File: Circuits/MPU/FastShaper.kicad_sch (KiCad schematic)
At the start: 34 parts, among them U35 ADA4805-2ARMZ, U36 ADA4805-2ARMZ

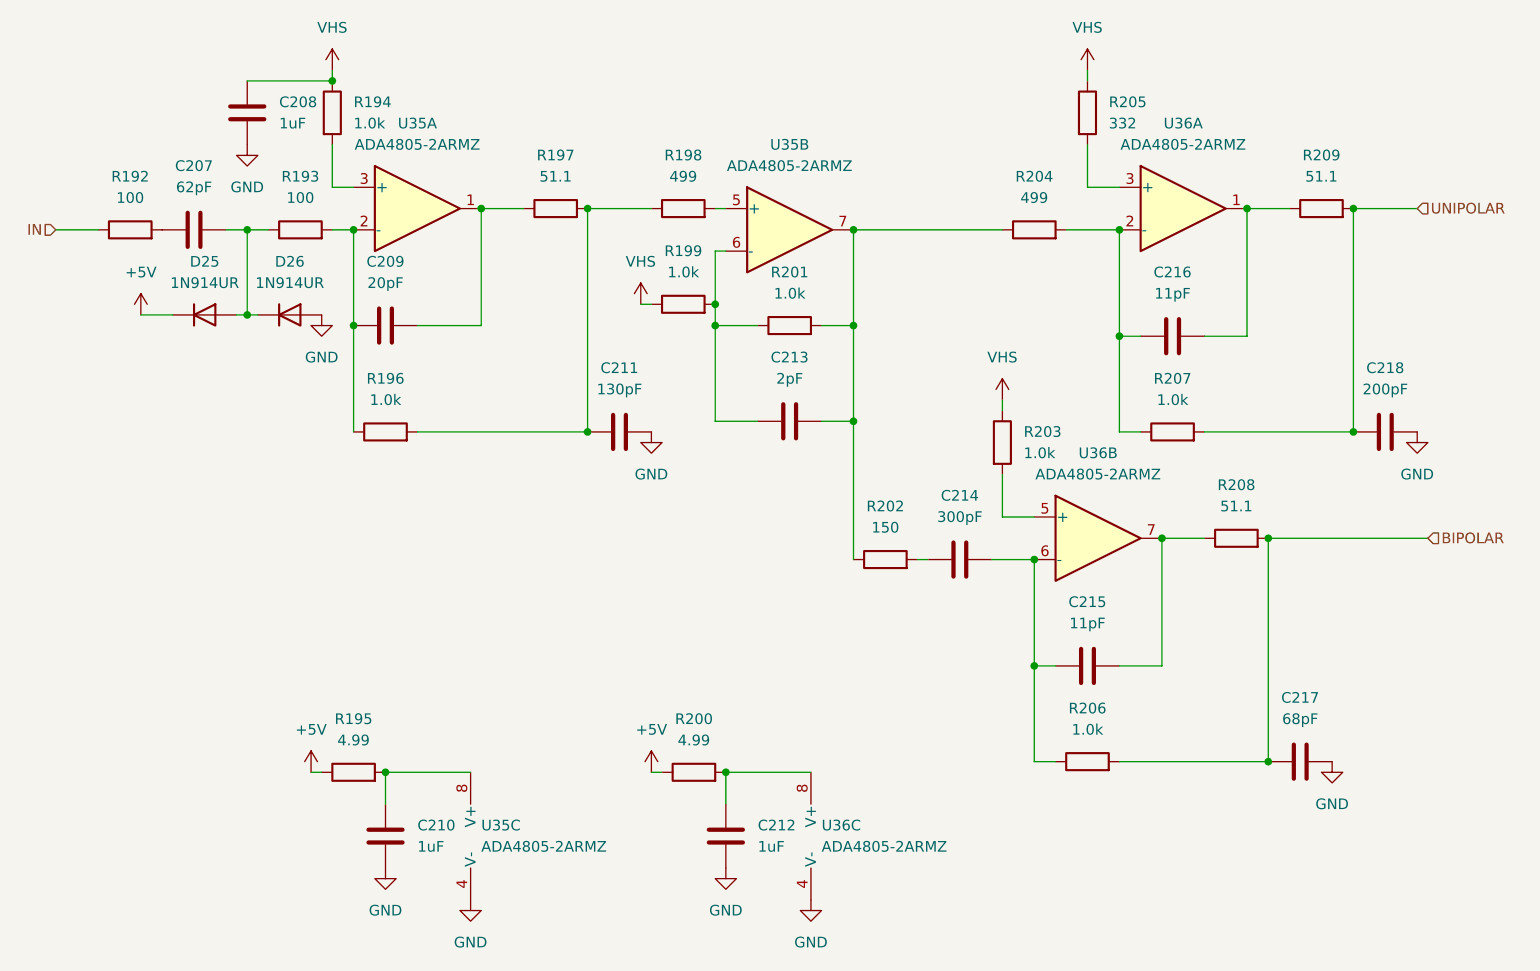
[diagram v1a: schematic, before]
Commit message: Files changed due to KiCAD update
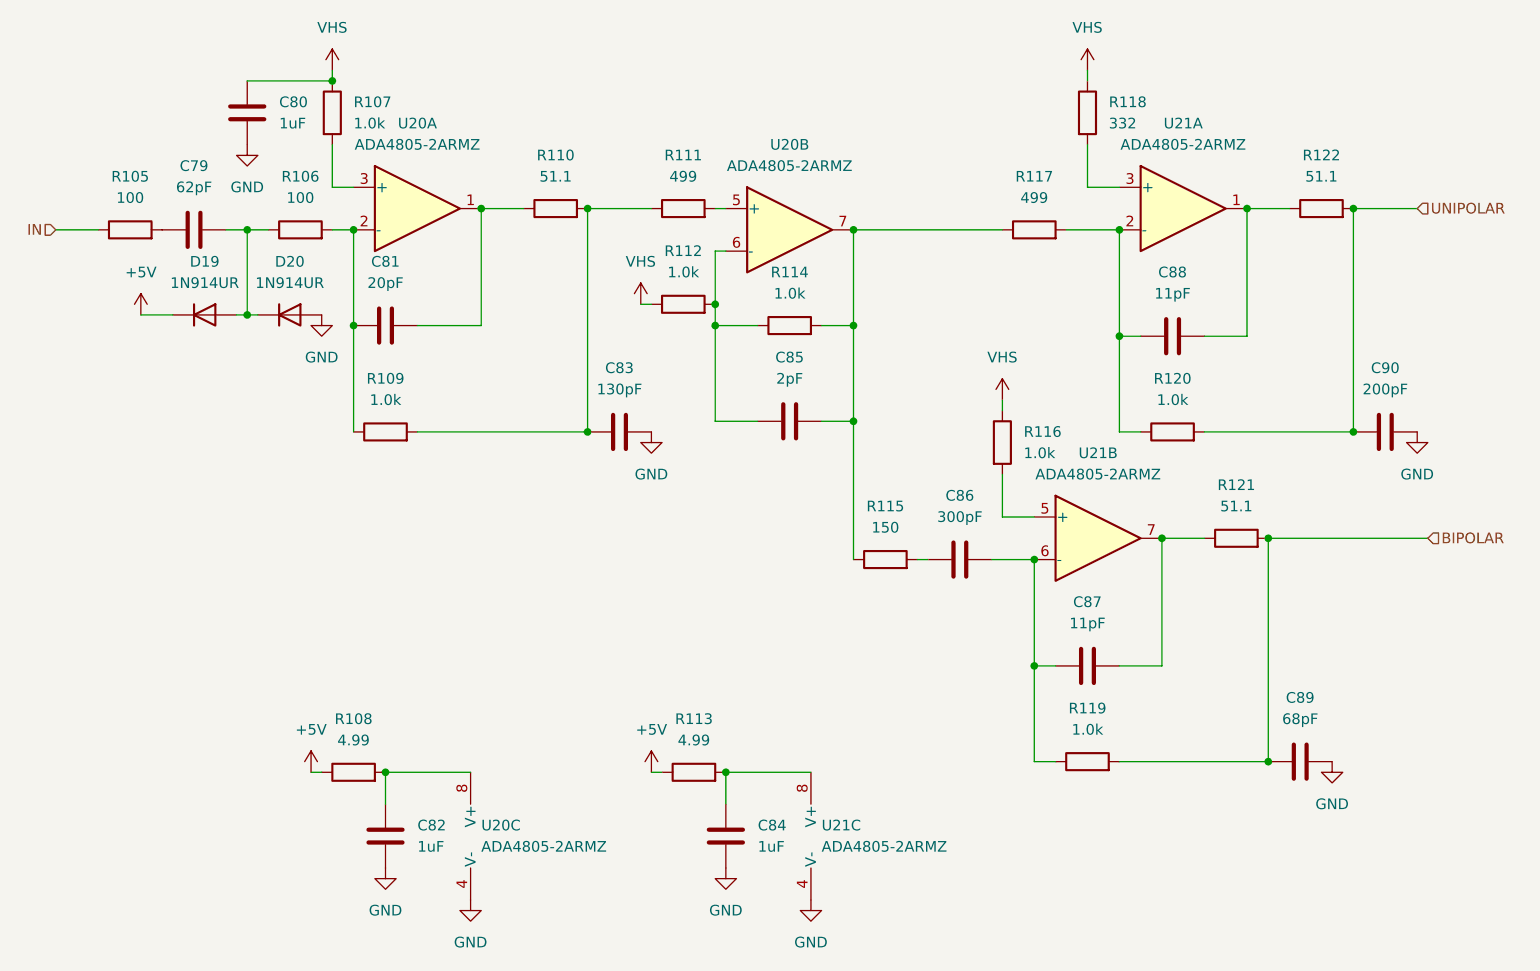
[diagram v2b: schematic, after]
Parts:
- renumbered C207 to C79, C208 to C80, C209 to C81, C210 to C82, C211 to C83, C212 to C84, C213 to C85, C214 to C86, C215 to C87, C216 to C88, C217 to C89, C218 to C90, D25 to D19, D26 to D20, R192 to R105, R193 to R106, R194 to R107, R195 to R108, R196 to R109, R197 to R110, R198 to R111, R199 to R112, R200 to R113, R201 to R114, R202 to R115, R203 to R116, R204 to R117, R205 to R118, R206 to R119, R207 to R120, R208 to R121, R209 to R122, U35 to U20, U36 to U21
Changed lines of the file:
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@@
 (kicad_sch
-	(version 20231120)
+	(version 20250114)
 	(generator "eeschema")
-	(generator_version "8.0")
+	(generator_version "9.0")
 	(paper "USLetter")
 	(title_block
@@
 		(shape input)
 		(at 204.47 66.04 0)
-		(fields_autoplaced yes)
 		(effects
 			(font
@@
 		(shape input)
 		(at 41.91 68.58 180)
-		(fields_autoplaced yes)
 		(effects
 			(font
@@
 		(shape input)
 		(at 205.74 105.41 0)
-		(fields_autoplaced yes)
 		(effects
 			(font
@@
 		(dnp no)
 		(fields_autoplaced yes)
-		(property "Reference" "D26"
+		(property "Reference" "D20"
 			(at 69.85 72.39 0)
 			(effects
@@
 		(dnp no)
 		(fields_autoplaced yes)
-		(property "Reference" "U35"
+		(property "Reference" "U20"
 			(at 85.09 55.88 0)
 			(effects
@@
 		(dnp no)
 		(fields_autoplaced yes)
-		(property "Reference" "#PWR0309"
+		(property "Reference" "#PWR0191"
 			(at 132.08 154.94 0)
 			(effects
@@
 		(dnp no)
 		(fields_autoplaced yes)
-		(property "Reference" "#PWR0298"
+		(property "Reference" "#PWR0180"
 			(at 52.07 82.55 0)
 			(effects
@@
 		(dnp no)
 		(fields_autoplaced yes)
-		(property "Reference" "#PWR0310"
+		(property "Reference" "#PWR0192"
 			(at 154.94 92.71 0)
 			(effects
@@
 		(dnp no)
 		(fields_autoplaced yes)
-		(property "Reference" "#PWR0306"
+		(property "Reference" "#PWR0188"
 			(at 113.03 99.06 0)
 			(effects
@@
 		(dnp no)
 		(fields_autoplaced yes)
-		(property "Reference" "R204"
+		(property "Reference" "R117"
 			(at 158.75 62.23 90)
 			(effects
@@
 		(dnp no)
 		(fields_autoplaced yes)
-		(property "Reference" "#PWR0312"
+		(property "Reference" "#PWR0194"
 			(at 194.31 138.43 0)
 			(effects
@@
 		(dnp no)
 		(fields_autoplaced yes)
-		(property "Reference" "U35"
+		(property "Reference" "U20"
 			(at 92.71 139.7 0)
 			(effects
@@
 		(dnp no)
 		(fields_autoplaced yes)
-		(property "Reference" "U36"
+		(property "Reference" "U21"
 			(at 133.35 139.7 0)
 			(effects
@@
 		(dnp no)
 		(fields_autoplaced yes)
-		(property "Reference" "R207"
+		(property "Reference" "R120"
 			(at 175.26 86.36 90)
 			(effects
@@
 		(dnp no)
 		(fields_autoplaced yes)
-		(property "Reference" "C216"
+		(property "Reference" "C88"
 			(at 175.26 73.66 90)
 			(effects
@@
 		(dnp no)
 		(fields_autoplaced yes)
-		(property "Reference" "R205"
+		(property "Reference" "R118"
 			(at 167.64 53.34 0)
 			(effects
@@
 		(dnp no)
 		(fields_autoplaced yes)
-		(property "Reference" "D25"
+		(property "Reference" "D19"
 			(at 59.69 72.39 0)
 			(effects
@@
 		(dnp no)
 		(fields_autoplaced yes)
-		(property "Reference" "C212"
+		(property "Reference" "C84"
 			(at 125.73 139.7 0)
 			(effects
@@
 		(dnp no)
 		(fields_autoplaced yes)
-		(property "Reference" "R209"
+		(property "Reference" "R122"
 			(at 193.04 59.69 90)
 			(effects
@@
 		(dnp no)
 		(fields_autoplaced yes)
-		(property "Reference" "R198"
+		(property "Reference" "R111"
 			(at 116.84 59.69 90)
 			(effects
@@
 		(dnp no)
 		(fields_autoplaced yes)
-		(property "Reference" "U36"
+		(property "Reference" "U21"
 			(at 176.53 55.88 0)
 			(effects
@@
 		(dnp no)
 		(fields_autoplaced yes)
-		(property "Reference" "#PWR0303"
+		(property "Reference" "#PWR0185"
 			(at 81.28 151.13 0)
 			(effects
@@
 		(dnp no)
 		(fields_autoplaced yes)
-		(property "Reference" "R195"
+		(property "Reference" "R108"
 			(at 77.47 127 90)
 			(effects
@@
 		(dnp no)
 		(fields_autoplaced yes)
-		(property "Reference" "#PWR0299"
+		(property "Reference" "#PWR0181"
 			(at 64.77 64.77 0)
 			(effects
@@
 		(dnp no)
 		(fields_autoplaced yes)
-		(property "Reference" "C217"
+		(property "Reference" "C89"
 			(at 190.5 124.46 90)
 			(effects
@@
 		(dnp no)
 		(fields_autoplaced yes)
-		(property "Reference" "#PWR0300"
+		(property "Reference" "#PWR0182"
 			(at 72.39 137.16 0)
 			(effects
@@
 		(dnp no)
 		(fields_autoplaced yes)
-		(property "Reference" "R208"
+		(property "Reference" "R121"
 			(at 182.88 99.06 90)
 			(effects
@@
 		(dnp no)
 		(fields_autoplaced yes)
-		(property "Reference" "R203"
+		(property "Reference" "R116"
 			(at 157.48 92.71 0)
 			(effects
@@
 		(dnp no)
 		(fields_autoplaced yes)
-		(property "Reference" "C215"
+		(property "Reference" "C87"
 			(at 165.1 113.03 90)
 			(effects
@@
 		(dnp no)
 		(fields_autoplaced yes)
-		(property "Reference" "R193"
+		(property "Reference" "R106"
 			(at 71.12 62.23 90)
 			(effects
@@
 		(dnp no)
 		(fields_autoplaced yes)
-		(property "Reference" "R192"
+		(property "Reference" "R105"
 			(at 50.8 62.23 90)
 			(effects
@@
 		(dnp no)
 		(fields_autoplaced yes)
-		(property "Reference" "R196"
+		(property "Reference" "R109"
 			(at 81.28 86.36 90)
 			(effects
@@
 		(dnp no)
 		(fields_autoplaced yes)
-		(property "Reference" "C213"
+		(property "Reference" "C85"
 			(at 129.54 83.82 90)
 			(effects
@@
 		(dnp no)
 		(fields_autoplaced yes)
-		(property "Reference" "#PWR0307"
+		(property "Reference" "#PWR0189"
 			(at 113.03 137.16 0)
 			(effects
@@
 		(dnp no)
 		(fields_autoplaced yes)
-		(property "Reference" "U35"
+		(property "Reference" "U20"
 			(at 129.54 58.42 0)
 			(effects
@@
 		(dnp no)
 		(fields_autoplaced yes)
-		(property "Reference" "#PWR0313"
+		(property "Reference" "#PWR0195"
 			(at 204.47 99.06 0)
 			(effects
@@
 		(dnp no)
 		(fields_autoplaced yes)
-		(property "Reference" "R197"
+		(property "Reference" "R110"
 			(at 101.6 59.69 90)
 			(effects
@@
 		(dnp no)
 		(fields_autoplaced yes)
-		(property "Reference" "R201"
+		(property "Reference" "R114"
 			(at 129.54 73.66 90)
 			(effects
@@
 		(dnp no)
 		(fields_autoplaced yes)
-		(property "Reference" "R199"
+		(property "Reference" "R112"
 			(at 116.84 71.12 90)
 			(effects
@@
 		(dnp no)
 		(fields_autoplaced yes)
-		(property "Reference" "R206"
+		(property "Reference" "R119"
 			(at 165.1 125.73 90)
 			(effects
@@
 		(dnp no)
 		(fields_autoplaced yes)
-		(property "Reference" "R202"
+		(property "Reference" "R115"
 			(at 140.97 101.6 90)
 			(effects
@@
 		(dnp no)
 		(fields_autoplaced yes)
-		(property "Reference" "#PWR0305"
+		(property "Reference" "#PWR0187"
 			(at 111.76 81.28 0)
 			(effects
@@
 		(dnp no)
 		(fields_autoplaced yes)
-		(property "Reference" "C208"
+		(property "Reference" "C80"
 			(at 68.58 53.34 0)
 			(effects
@@
 		(dnp no)
 		(fields_autoplaced yes)
-		(property "Reference" "#PWR0308"
+		(property "Reference" "#PWR0190"
 			(at 121.92 151.13 0)
 			(effects
@@
 		(dnp no)
 		(fields_autoplaced yes)
-		(property "Reference" "C218"
+		(property "Reference" "C90"
 			(at 200.66 85.09 90)
 			(effects
@@
 		(dnp no)
 		(fields_autoplaced yes)
-		(property "Reference" "C214"
+		(property "Reference" "C86"
 			(at 149.86 100.33 90)
 			(effects
@@
 		(dnp no)
 		(fields_autoplaced yes)
-		(property "Reference" "U36"
+		(property "Reference" "U21"
 			(at 166.37 95.25 0)
 			(effects
@@
 		(dnp no)
 		(fields_autoplaced yes)
-		(property "Reference" "#PWR0301"
+		(property "Reference" "#PWR0183"
 			(at 73.66 85.09 0)
 			(effects
@@
 		(dnp no)
 		(fields_autoplaced yes)
-		(property "Reference" "#PWR0311"
+		(property "Reference" "#PWR0193"
 			(at 165.1 53.34 0)
 			(effects
@@
 		(dnp no)
 		(fields_autoplaced yes)
-		(property "Reference" "R194"
+		(property "Reference" "R107"
 			(at 77.47 53.34 0)
 			(effects
@@
 		(dnp no)
 		(fields_autoplaced yes)
-		(property "Reference" "C211"
+		(property "Reference" "C83"
 			(at 109.22 85.09 90)
 			(effects
@@
 		(dnp no)
 		(fields_autoplaced yes)
-		(property "Reference" "R200"
+		(property "Reference" "R113"
 			(at 118.11 127 90)
 			(effects
@@
 		(dnp no)
 		(fields_autoplaced yes)
-		(property "Reference" "C209"
+		(property "Reference" "C81"
 			(at 81.28 72.39 90)
 			(effects
@@
 		(dnp no)
 		(fields_autoplaced yes)
-		(property "Reference" "C207"
+		(property "Reference" "C79"
 			(at 58.42 60.96 90)
 			(effects
@@
 		(dnp no)
 		(fields_autoplaced yes)
-		(property "Reference" "#PWR0304"
+		(property "Reference" "#PWR0186"
 			(at 91.44 154.94 0)
 			(effects
@@
 		(dnp no)
 		(fields_autoplaced yes)
-		(property "Reference" "#PWR0302"
+		(property "Reference" "#PWR0184"
 			(at 74.93 53.34 0)
 			(effects
@@
 		(dnp no)
 		(fields_autoplaced yes)
-		(property "Reference" "C210"
+		(property "Reference" "C82"
 			(at 85.09 139.7 0)
 			(effects

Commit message: component values for 150 ns fast shaping
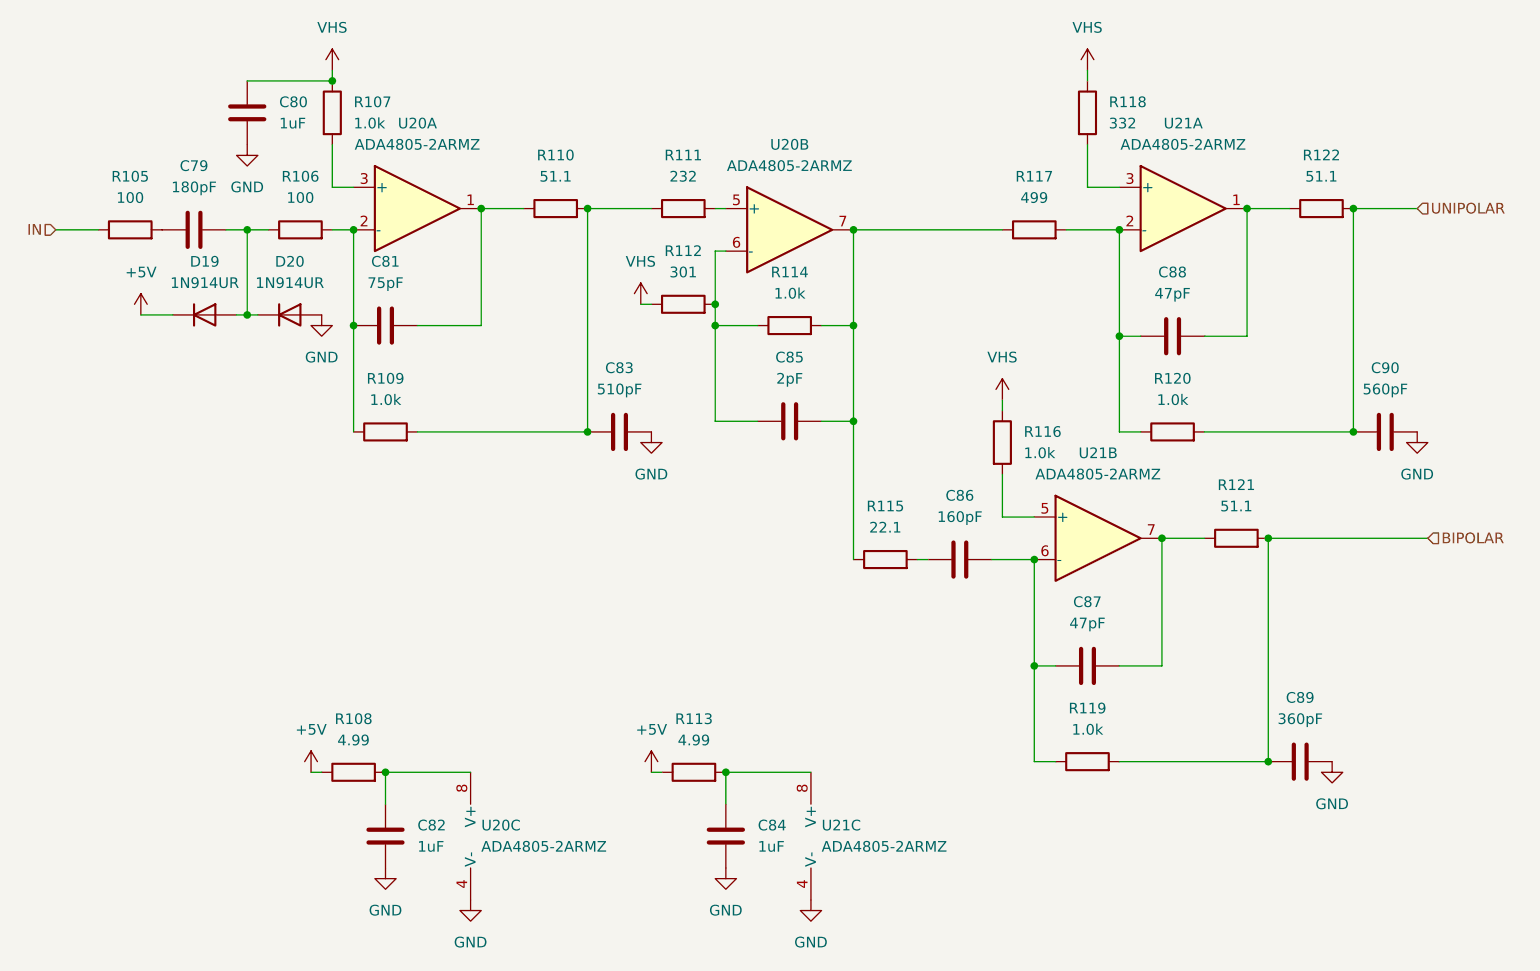
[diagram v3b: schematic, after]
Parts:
- C79: value 62pF -> 180pF
- C81: value 20pF -> 75pF
- C83: value 130pF -> 510pF
- C86: value 300pF -> 160pF
- C87, C88: value 11pF -> 47pF
- C89: value 68pF -> 360pF
- C90: value 200pF -> 560pF
- R111: value 499 -> 232
- R112: value 1.0k -> 301
- R115: value 150 -> 22.1
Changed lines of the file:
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@@
 			)
 		)
-		(property "Value" "11pF"
+		(property "Value" "47pF"
 			(at 175.26 76.2 90)
 			(effects
@@
 			)
 		)
-		(property "Value" "499"
+		(property "Value" "232"
 			(at 116.84 62.23 90)
 			(effects
@@
 			)
 		)
-		(property "Value" "68pF"
+		(property "Value" "360pF"
 			(at 190.5 127 90)
 			(effects
@@
 			)
 		)
-		(property "Value" "11pF"
+		(property "Value" "47pF"
 			(at 165.1 115.57 90)
 			(effects
@@
 			)
 		)
-		(property "Value" "1.0k"
+		(property "Value" "301"
 			(at 116.84 73.66 90)
 			(effects
@@
 			)
 		)
-		(property "Value" "150"
+		(property "Value" "22.1"
 			(at 140.97 104.14 90)
 			(effects
@@
 			)
 		)
-		(property "Value" "200pF"
+		(property "Value" "560pF"
 			(at 200.66 87.63 90)
 			(effects
@@
 			)
 		)
-		(property "Value" "300pF"
+		(property "Value" "160pF"
 			(at 149.86 102.87 90)
 			(effects
@@
 			)
 		)
-		(property "Value" "130pF"
+		(property "Value" "510pF"
 			(at 109.22 87.63 90)
 			(effects
@@
 			)
 		)
-		(property "Value" "20pF"
+		(property "Value" "75pF"
 			(at 81.28 74.93 90)
 			(effects
@@
 			)
 		)
-		(property "Value" "62pF"
+		(property "Value" "180pF"
 			(at 58.42 63.5 90)
 			(effects
